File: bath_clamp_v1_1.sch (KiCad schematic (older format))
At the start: 76 parts, among them J1 105-1103-001, J2 105-1103-001, J3 105-1103-001, J4 HDMI_A, K1 1462042-8, K2 1462042-8, Q1 MBT3904DW1T1G, Q3 MBT3904DW1T1G, Q4 MBT3904DW1T1G, U1 OPA828, U12 TCA9555DBR, U13 TCA9555DBR, U19 TMUX6136PWR, U2 ADG1208, U25 OPA2156xD, U3 G6L-1F-TR-DC5, U4 G6L-1F-TR-DC5, U5 G6L-1F-TR-DC5, U8 OPA2156xD

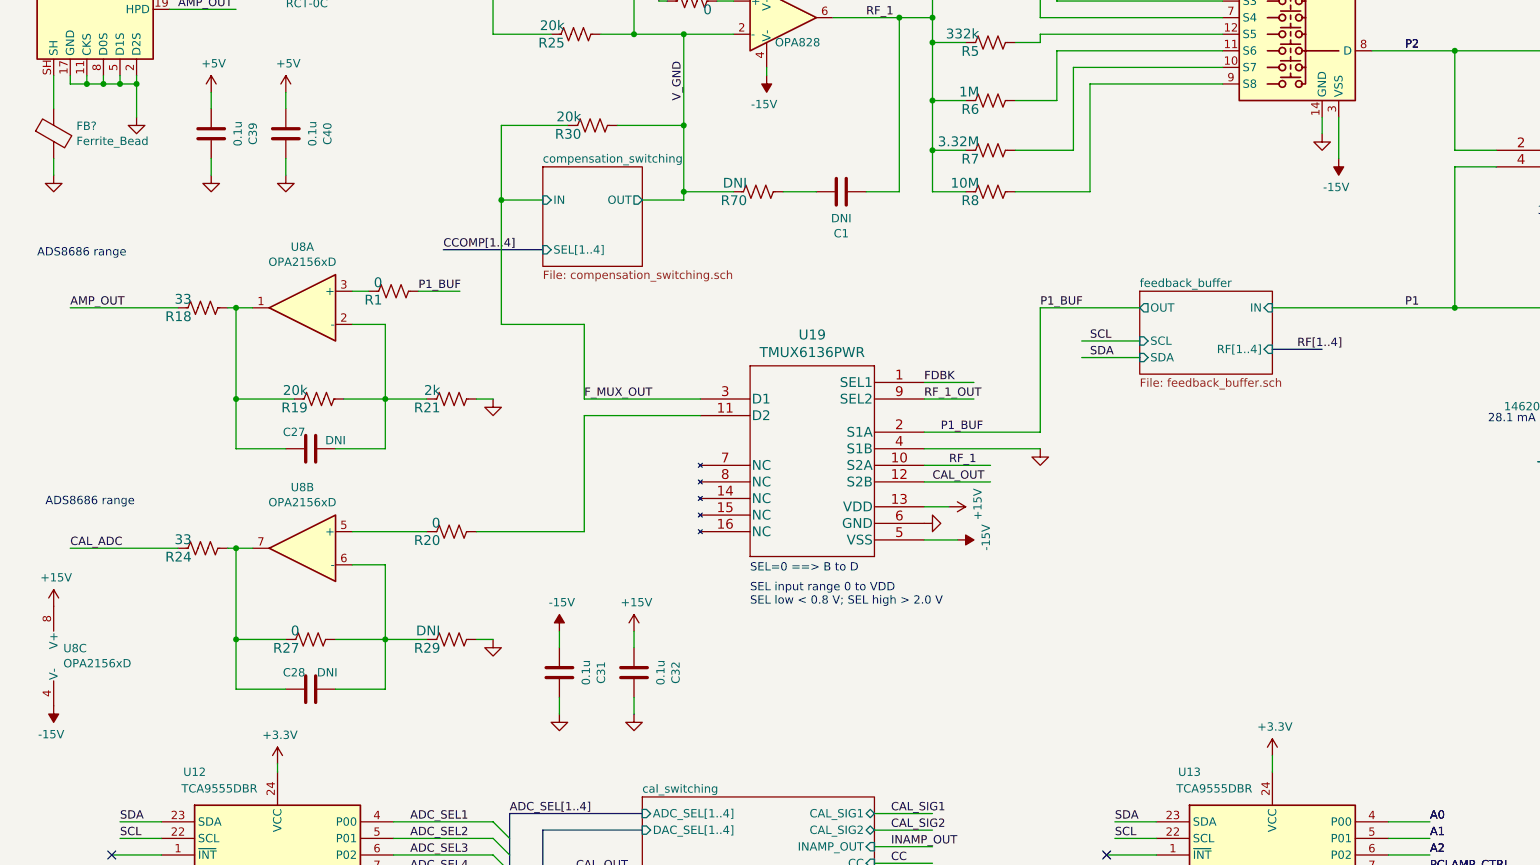
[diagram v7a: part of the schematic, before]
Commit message: clamp files at submission to JLCPCB
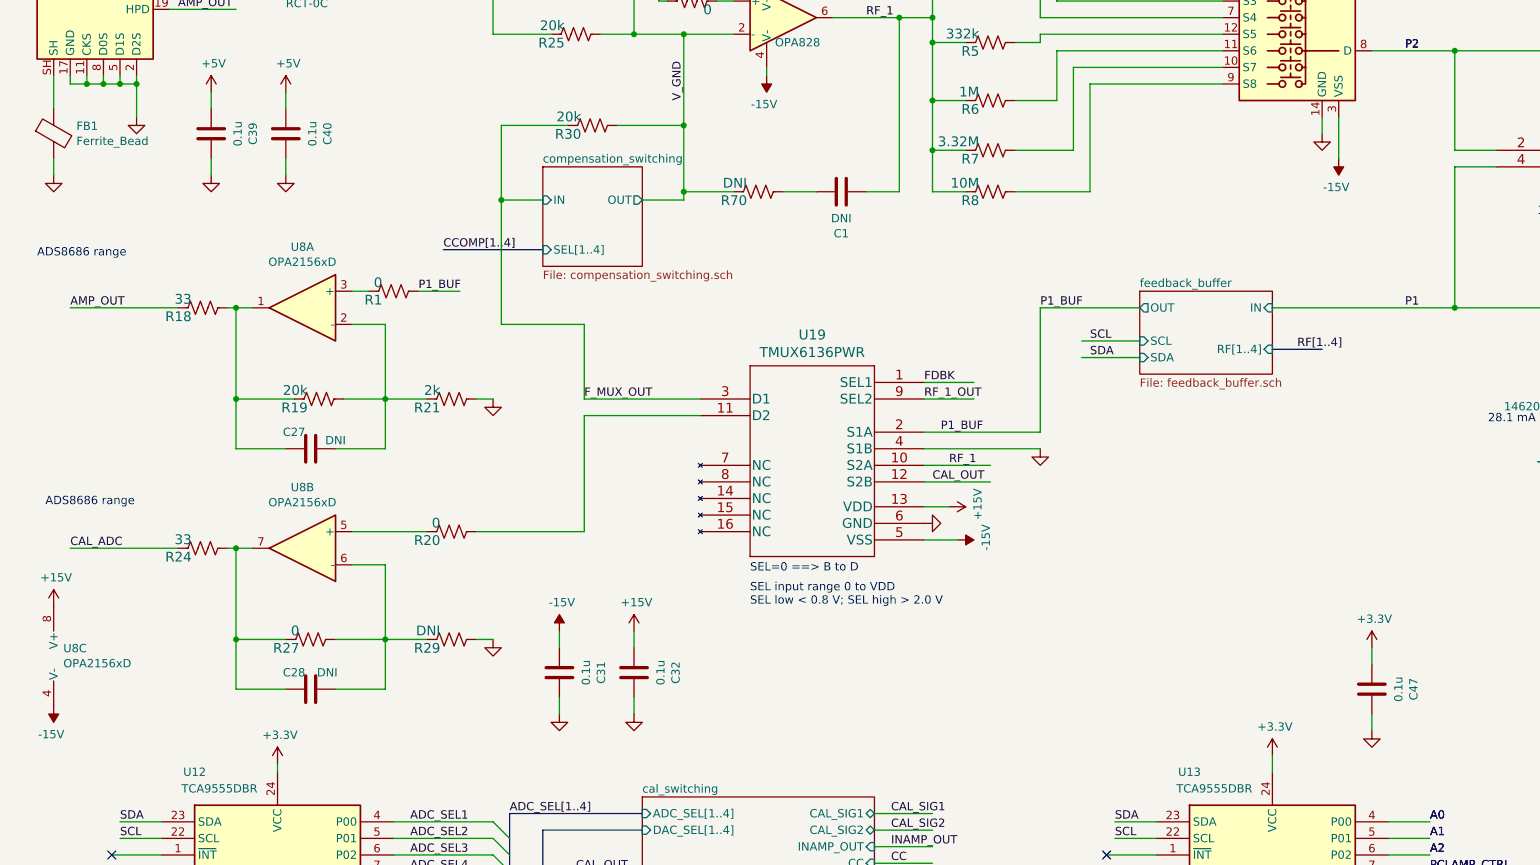
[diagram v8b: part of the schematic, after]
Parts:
- added C47: 0.1u, Capacitor_SMD:C_0603_1608Metric, symbol Device:C
- gave numbers to parts that had none: 1
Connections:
- wire segments 358 -> 360
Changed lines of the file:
@@
 Connection ~ 1250 3600
 $Comp
-L Device:Ferrite_Bead FB?
+L Device:Ferrite_Bead FB1
 U 1 1 61B9C943
 P 750 3900
-F 0 "FB?" H 887 3946 50  0000 L CNN
+F 0 "FB1" H 887 3946 50  0000 L CNN
 F 1 "Ferrite_Bead" H 887 3855 50  0000 L CNN
 F 2 "Capacitor_SMD:C_1206_3216Metric" V 680 3900 50  0001 C CNN
@@
 $EndComp
 $Comp
-L power:GND #PWR?
+L power:GND #PWR0196
 U 1 1 61B9CF45
 P 750 4150
-AR Path="/6032F251/61B9CF45" Ref="#PWR?"  Part="1"
+AR Path="/6032F251/61B9CF45" Ref="#PWR0196"  Part="1"
 AR Path="/6032F251/608FDC40/61B9CF45" Ref="#PWR?"  Part="1"
-F 0 "#PWR?" H 750 3900 50  0001 C CNN
+F 0 "#PWR0196" H 750 3900 50  0001 C CNN
 F 1 "GND" V 755 4022 50  0001 R CNN
 F 2 "" H 750 4150 50  0001 C CNN
@@
 Wire Wire Line
 	750  3550 750  3750
+$Comp
+L power:GND #PWR0205
+U 1 1 60F790A6
+P 8700 7500
+AR Path="/6032F251/60F790A6" Ref="#PWR0205"  Part="1"
+AR Path="/6032F251/608FDC40/60F790A6" Ref="#PWR?"  Part="1"
+F 0 "#PWR0205" H 8700 7250 50  0001 C CNN
+F 1 "GND" V 8705 7372 50  0001 R CNN
+F 2 "" H 8700 7500 50  0001 C CNN
+F 3 "" H 8700 7500 50  0001 C CNN
+	1    8700 7500
+	1    0    0    -1
+$EndComp
+$Comp
+L Device:C C47
+U 1 1 60F790AE
+P 8700 7250
+AR Path="/6032F251/60F790AE" Ref="C47"  Part="1"
+AR Path="/6032F251/608FDC40/60F790AE" Ref="C?"  Part="1"
+F 0 "C47" V 8448 7250 50  0000 C CNN
+F 1 "0.1u" V 8539 7250 50  0000 C CNN
+F 2 "Capacitor_SMD:C_0603_1608Metric" H 8738 7100 50  0001 C CNN
+F 3 "~" H 8700 7250 50  0001 C CNN
+F 4 "CC0603MRX7R8BB104" H 8448 7350 50  0001 C CNN "Manf#"
+F 5 "25V" H 8448 7350 50  0001 C CNN "voltage"
+	1    8700 7250
+	-1   0    0    1
+$EndComp
+Wire Wire Line
+	8700 7500 8700 7400
+Wire Wire Line
+	8700 7100 8700 7000
 Wire Bus Line
 	9200 9450 9200 9750
@@
 Wire Bus Line
 	3500 8000 3500 8450
+$Comp
+L power:+3.3V #PWR0206
+U 1 1 60FA3837
+P 8700 7000
+F 0 "#PWR0206" H 8700 6850 50  0001 C CNN
+F 1 "+3.3V" H 8715 7173 50  0000 C CNN
+F 2 "" H 8700 7000 50  0001 C CNN
+F 3 "" H 8700 7000 50  0001 C CNN
+	1    8700 7000
+	1    0    0    -1
+$EndComp
 $EndSCHEMATC
